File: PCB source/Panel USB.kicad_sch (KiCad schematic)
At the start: 9 parts, among them J4 Connector, USB-TYPE-C-16P, U12 IP4234CZ6

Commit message: Pass ERC
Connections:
- net FRONT_PANEL.D+ renamed FRONT_PANEL.+
- net FRONT_PANEL.D- renamed FRONT_PANEL.-
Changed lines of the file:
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@@
 		)
 	)
-	(label "FRONT_PANEL.D+"
+	(label "FRONT_PANEL.+"
 		(at 194.31 99.06 180)
 		(fields_autoplaced yes)
@@
 		)
 	)
-	(label "FRONT_PANEL.D-"
+	(label "FRONT_PANEL.-"
 		(at 194.31 101.6 180)
 		(fields_autoplaced yes)

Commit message: Prepare board for layout
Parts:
- removed J4: Connector, USB-TYPE-C-16P, USB_C_Upright16pin:MOLEX_2169890001, symbol PCM_JLCPCB-Extended:Connector, USB-TYPE-C-16P
- added J5: Connector, USB-TYPE-C-16P, PCM_JLCPCB:TYPE-C-SMD_HX-TYPE-C-16PIN, symbol PCM_JLCPCB-Extended:Connector, USB-TYPE-C-16P
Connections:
- net GND: now also J5.A12B1 (GND), J5.B12A1 (GND)
- net VBUS_IN: now also J5.A9B4 (VBUS), J5.B9A4 (VBUS)
- net at C55.1, R31.1: now also J5.S1 (SHIELD)
- net at R29.1: now also J5.A7 (D-), J5.B7 (D-)
- net at R28.1: now also J5.A5 (CC1)
- net at R30.1: now also J5.A6 (D+), J5.B6 (D+)
- net at R27.1: now also J5.B5 (CC2)
- net FRONT_PANEL.+ renamed FRONT_PANEL.D-
- net FRONT_PANEL.- renamed FRONT_PANEL.D+
- net USB_IN.+ renamed USB_IN.D+
- net USB_IN.- renamed USB_IN.D-
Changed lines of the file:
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@@
 		)
 	)
-	(label "FRONT_PANEL.+"
-		(at 194.31 99.06 180)
+	(label "FRONT_PANEL.D+"
+		(at 193.04 101.6 180)
+		(fields_autoplaced yes)
+		(effects
+			(font
+				(size 1.27 1.27)
+			)
+			(justify right bottom)
+		)
+	)
+	(label "FRONT_PANEL.D-"
+		(at 193.04 99.06 180)
 		(fields_autoplaced yes)
 		(effects
@@
 		)
 	)
-	(label "USB_IN.+"
+	(label "USB_IN.D+"
 		(at 140.97 88.9 180)
 		(fields_autoplaced yes)
@@
 		)
 	)
-	(label "FRONT_PANEL.-"
-		(at 194.31 101.6 180)
-		(fields_autoplaced yes)
-		(effects
-			(font
-				(size 1.27 1.27)
-			)
-			(justify right bottom)
-		)
-	)
-	(label "USB_IN.-"
+	(label "USB_IN.D-"
 		(at 140.97 83.82 180)
 		(fields_autoplaced yes)
@@
 	)
 	(symbol
-		(lib_id "PCM_JLCPCB-Extended:Connector, USB-TYPE-C-16P")
-		(at 96.52 85.09 0)
-		(unit 1)
-		(exclude_from_sim no)
-		(in_bom yes)
-		(on_board yes)
-		(dnp no)
-		(fields_autoplaced yes)
-		(property "Reference" "J4"
-			(at 96.52 64.77 0)
-			(effects
-				(font
-					(size 1.27 1.27)
-				)
-			)
-		)
-		(property "Value" "Connector, USB-TYPE-C-16P"
-			(at 99.06 86.36 0)
-			(effects
-				(font
-					(size 1.27 1.27)
-				)
-				(hide yes)
-			)
-		)
-		(property "Footprint" "USB_C_Upright16pin:MOLEX_2169890001"
-			(at 96.52 95.25 0)
-			(effects
-				(font
-					(size 1.27 1.27)
-					(italic yes)
-				)
-				(hide yes)
-			)
-		)
-		(property "Datasheet" "https://atta.szlcsc.com/upload/public/pdf/source/20220920/0EF8F885FCCEA71F60E9E85152155021.pdf"
-			(at 94.234 84.963 0)
-			(effects
-				(font
-					(size 1.27 1.27)
-				)
-				(justify left)
-				(hide yes)
-			)
-		)
-		(property "Description" "3A 1 Horizontal attachment 16P Female -25℃~+85℃ Type-C SMD USB Connectors ROHS"
-			(at 99.06 83.82 0)
-			(effects
-				(font
-					(size 1.27 1.27)
-				)
-				(hide yes)
-			)
-		)
-		(property "LCSC" "C2927039"
-			(at 99.06 83.82 0)
-			(effects
-				(font
-					(size 1.27 1.27)
-				)
-				(hide yes)
-			)
-		)
-		(pin "A8"
-		)
-		(pin "B6"
-		)
-		(pin "B5"
-		)
-		(pin "A5"
-		)
-		(pin "A7"
-		)
-		(pin "A6"
-		)
-		(pin "B7"
-		)
-		(pin "B8"
-		)
-		(pin "S1"
-		)
-		(pin "A12B1"
-		)
-		(pin "B9A4"
-		)
-		(pin "B12A1"
-		)
-		(pin "A9B4"
-		)
-		(instances
-			(project "OrangePie"
-				(path "/3103c9de-f1ba-4d51-8bfc-798df1c75e2f/86d81324-cbad-4692-8b67-2c038a3e8215"
-					(reference "J4")
-					(unit 1)
-				)
-			)
-		)
-	)
-	(symbol
 		(lib_id "power:GND")
 		(at 96.52 125.73 0)
@@
 					(unit 1)
 				)
+			)
+		)
+	)
+	(symbol
+		(lib_id "PCM_JLCPCB-Extended:Connector, USB-TYPE-C-16P")
+		(at 96.52 85.09 0)
+		(unit 1)
+		(exclude_from_sim no)
+		(in_bom yes)
+		(on_board yes)
+		(dnp no)
+		(fields_autoplaced yes)
+		(property "Reference" "J5"
+			(at 96.52 64.77 0)
+			(effects
+				(font
+					(size 1.27 1.27)
+				)
+			)
+		)
+		(property "Value" "Connector, USB-TYPE-C-16P"
+			(at 99.06 86.36 0)
+			(effects
+				(font
+					(size 1.27 1.27)
+				)
+				(hide yes)
+			)
+		)
+		(property "Footprint" "PCM_JLCPCB:TYPE-C-SMD_HX-TYPE-C-16PIN"
+			(at 96.52 95.25 0)
+			(effects
+				(font
+					(size 1.27 1.27)
+					(italic yes)
+				)
+				(hide yes)
+			)
+		)
+		(property "Datasheet" "https://atta.szlcsc.com/upload/public/pdf/source/20220920/0EF8F885FCCEA71F60E9E85152155021.pdf"
+			(at 94.234 84.963 0)
+			(effects
+				(font
+					(size 1.27 1.27)
+				)
+				(justify left)
+				(hide yes)
+			)
+		)
+		(property "Description" "3A 1 Horizontal attachment 16P Female -25℃~+85℃ Type-C SMD USB Connectors ROHS"
+			(at 99.06 83.82 0)
+			(effects
+				(font
+					(size 1.27 1.27)
+				)
+				(hide yes)
+			)
+		)
+		(property "LCSC" "C2927039"
+			(at 99.06 83.82 0)
+			(effects
+				(font
+					(size 1.27 1.27)
+				)
+				(hide yes)
+			)
+		)
+		(pin "A6"
+		)
+		(pin "A12B1"
+		)
+		(pin "S1"
+		)
+		(pin "B8"
+		)
+		(pin "B12A1"
+		)
+		(pin "A9B4"
+		)
+		(pin "A7"
+		)
+		(pin "A5"
+		)
+		(pin "A8"
+		)
+		(pin "B6"
+		)
+		(pin "B7"
+		)
+		(pin "B9A4"
+		)
+		(pin "B5"
+		)
+		(instances
+			(project ""
+				(path "/3103c9de-f1ba-4d51-8bfc-798df1c75e2f/86d81324-cbad-4692-8b67-2c038a3e8215"
+					(reference "J5")
+					(unit 1)
+				)

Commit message: Create v1 floorplan
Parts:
- J5: footprint PCM_JLCPCB:TYPE-C-SMD_HX-TYPE-C-16PIN -> Connector_USB:USB_C_Receptacle_GCT_USB4105-xx-A_16P_TopMnt_Horizontal
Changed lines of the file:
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@@
 			)
 		)
-		(property "Footprint" "PCM_JLCPCB:TYPE-C-SMD_HX-TYPE-C-16PIN"
+		(property "Footprint" "Connector_USB:USB_C_Receptacle_GCT_USB4105-xx-A_16P_TopMnt_Horizontal"
 			(at 96.52 95.25 0)
 			(effects

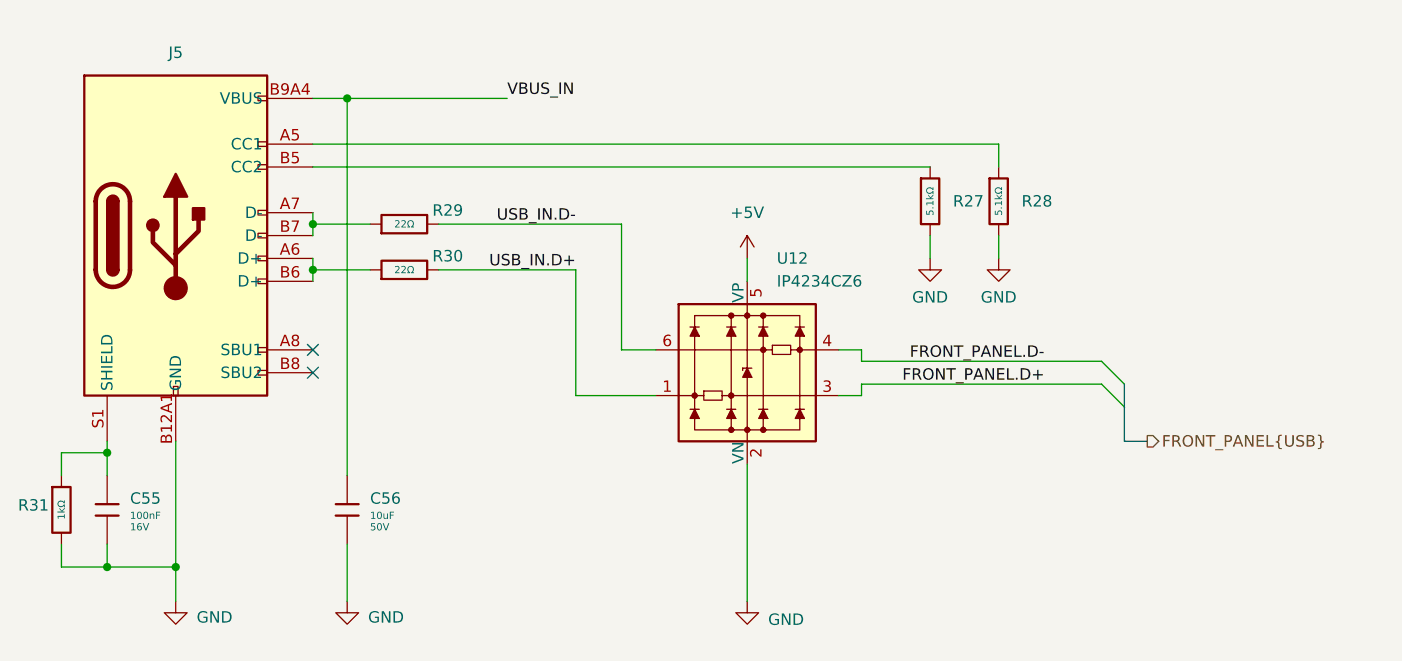
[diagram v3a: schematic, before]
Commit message: Do signal layer layout
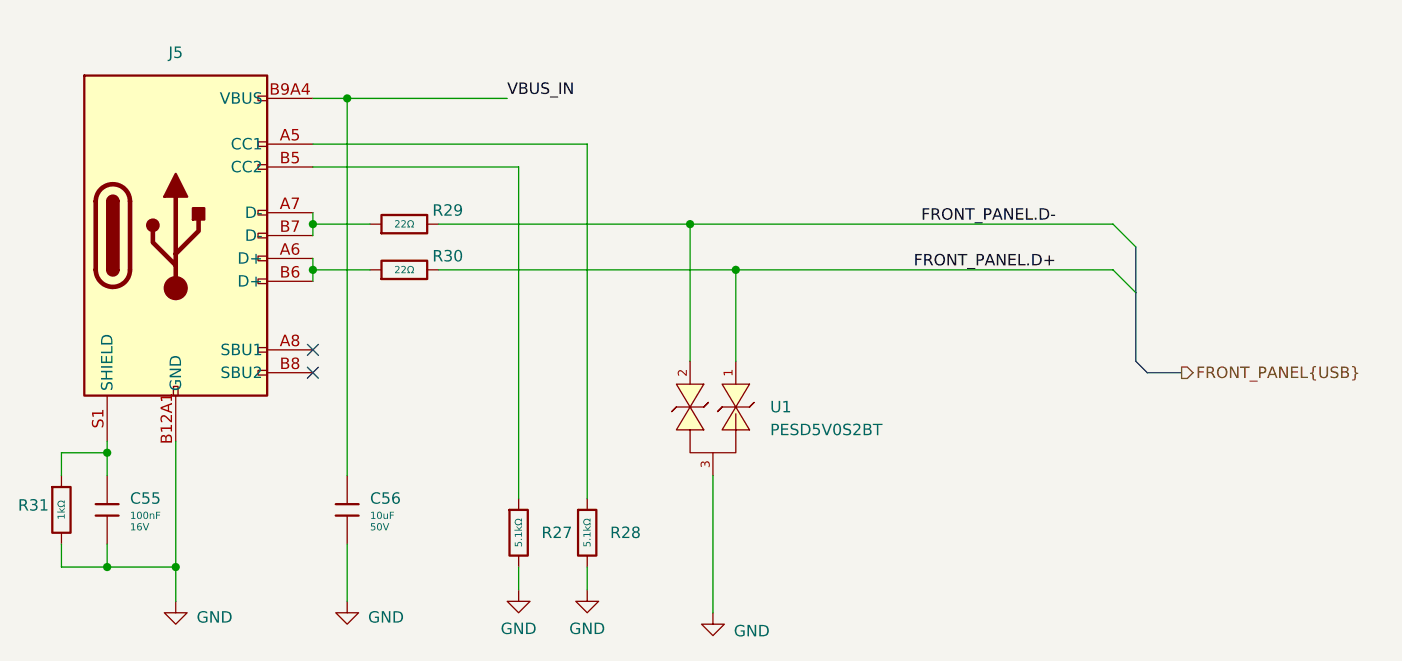
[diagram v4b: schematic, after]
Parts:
- removed U12: IP4234CZ6, Package_TO_SOT_SMD:SC-74-6_1.55x2.9mm_P0.95mm, symbol Power_Protection:IP4234CZ6
- added U1: PESD5V0S2BT, Package_TO_SOT_SMD:SOT-23, symbol PESD5V0S2BT:PESD5V0S2BT
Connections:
- net USB_IN.D+ is gone; now on net FRONT_PANEL.D+: R30.2
- net USB_IN.D- is gone; now on net FRONT_PANEL.D-: R29.2
- net FRONT_PANEL.D+: now also U1.1
- net FRONT_PANEL.D-: now also U1.2
- net GND: now also U1.3
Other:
- moved on the sheet: R27, R28

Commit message: Finish layout
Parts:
- removed J5: Connector, USB-TYPE-C-16P, Connector_USB:USB_C_Receptacle_GCT_USB4105-xx-A_16P_TopMnt_Horizontal, symbol PCM_JLCPCB-Extended:Connector, USB-TYPE-C-16P
- added J5: USB_C_Receptacle_USB2.0_16P, Connector_USB:USB_C_Receptacle_GCT_USB4105-xx-A_16P_TopMnt_Horizontal, symbol Connector:USB_C_Receptacle_USB2.0_16P
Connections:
- net GND: now also J5.A1 (GND), J5.A12 (GND), J5.B1 (GND), J5.B12 (GND)
- net VBUS_IN: now also J5.A4 (VBUS), J5.A9 (VBUS), J5.B4 (VBUS), J5.B9 (VBUS)
- net at C55.1, R31.1: now also J5.S1 (SHIELD)
- net at R29.1: now also J5.A7 (D-), J5.B7 (D-)
- net at R28.1: now also J5.A5 (CC1)
- net at R30.1: now also J5.A6 (D+), J5.B6 (D+)
- net at R27.1: now also J5.B5 (CC2)
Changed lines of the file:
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@@
-	)
-	(symbol
-		(lib_id "PCM_JLCPCB-Extended:Connector, USB-TYPE-C-16P")
-		(at 96.52 85.09 0)
-		(unit 1)
-		(exclude_from_sim no)
-		(in_bom yes)
-		(on_board yes)
-		(dnp no)
-		(fields_autoplaced yes)
-		(property "Reference" "J5"
-			(at 96.52 64.77 0)
-			(effects
-				(font
-					(size 1.27 1.27)
-				)
-			)
-		)
-		(property "Value" "Connector, USB-TYPE-C-16P"
-			(at 99.06 86.36 0)
-			(effects
-				(font
-					(size 1.27 1.27)
-				)
-				(hide yes)
-			)
-		)
-		(property "Footprint" "Connector_USB:USB_C_Receptacle_GCT_USB4105-xx-A_16P_TopMnt_Horizontal"
-			(at 96.52 95.25 0)
-			(effects
-				(font
-					(size 1.27 1.27)
-					(italic yes)
-				)
-				(hide yes)
-			)
-		)
-		(property "Datasheet" "https://atta.szlcsc.com/upload/public/pdf/source/20220920/0EF8F885FCCEA71F60E9E85152155021.pdf"
-			(at 94.234 84.963 0)
-			(effects
-				(font
-					(size 1.27 1.27)
-				)
-				(justify left)
-				(hide yes)
-			)
-		)
-		(property "Description" "3A 1 Horizontal attachment 16P Female -25℃~+85℃ Type-C SMD USB Connectors ROHS"
-			(at 99.06 83.82 0)
-			(effects
-				(font
-					(size 1.27 1.27)
-				)
-				(hide yes)
-			)
-		)
-		(property "LCSC" "C2927039"
-			(at 99.06 83.82 0)
-			(effects
-				(font
-					(size 1.27 1.27)
-				)
-				(hide yes)
-			)
-		)
-		(pin "A6"
-		)
-		(pin "A12B1"
-		)
-		(pin "S1"
-		)
-		(pin "B8"
-		)
-		(pin "B12A1"
-		)
-		(pin "A9B4"
-		)
-		(pin "A7"
-		)
-		(pin "A5"
-		)
-		(pin "A8"
-		)
-		(pin "B6"
-		)
-		(pin "B7"
-		)
-		(pin "B9A4"
-		)
-		(pin "B5"
-		)
-		(instances
-			(project ""
-				(path "/3103c9de-f1ba-4d51-8bfc-798df1c75e2f/86d81324-cbad-4692-8b67-2c038a3e8215"
-					(reference "J5")
-					(unit 1)
-				)
-			)
-		)
 	)
 	(symbol
@@
 					(unit 1)
 				)
+			)
+		)
+	)
+	(symbol
+		(lib_name "USB_C_Receptacle_USB2.0_16P_1")
+		(lib_id "Connector:USB_C_Receptacle_USB2.0_16P")
+		(at 96.52 85.09 0)
+		(unit 1)
+		(exclude_from_sim no)
+		(in_bom yes)
+		(on_board yes)
+		(dnp no)
+		(fields_autoplaced yes)
+		(property "Reference" "J5"
+			(at 96.52 62.23 0)
+			(effects
+				(font
+					(size 1.27 1.27)
+				)
+			)
+		)
+		(property "Value" "USB_C_Receptacle_USB2.0_16P"
+			(at 96.52 64.77 0)
+			(effects
+				(font
+					(size 1.27 1.27)
+				)
+			)
+		)
+		(property "Footprint" "Connector_USB:USB_C_Receptacle_GCT_USB4105-xx-A_16P_TopMnt_Horizontal"
+			(at 100.33 85.09 0)
+			(effects
+				(font
+					(size 1.27 1.27)
+				)
+				(hide yes)
+			)
+		)
+		(property "Datasheet" "https://www.usb.org/sites/default/files/documents/usb_type-c.zip"
+			(at 100.33 85.09 0)
+			(effects
+				(font
+					(size 1.27 1.27)
+				)
+				(hide yes)
+			)
+		)
+		(property "Description" "USB 2.0-only 16P Type-C Receptacle connector"
+			(at 96.52 85.09 0)
+			(effects
+				(font
+					(size 1.27 1.27)
+				)
+				(hide yes)
+			)
+		)
+		(pin "A4"
+		)
+		(pin "B9"
+		)
+		(pin "A8"
+		)
+		(pin "A9"
+		)
+		(pin "B1"
+		)
+		(pin "S1"
+		)
+		(pin "A1"
+		)
+		(pin "B12"
+		)
+		(pin "A7"
+		)
+		(pin "B6"
+		)
+		(pin "B8"
+		)
+		(pin "A5"
+		)
+		(pin "A6"
+		)
+		(pin "B5"
+		)
+		(pin "B4"
+		)
+		(pin "B7"
+		)
+		(pin "A12"
+		)
+		(instances
+			(project "OrangePie"
+				(path "/3103c9de-f1ba-4d51-8bfc-798df1c75e2f/86d81324-cbad-4692-8b67-2c038a3e8215"
+					(reference "J5")
+					(unit 1)
+				)

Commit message: Fix schematic
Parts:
- removed U1: PESD5V0S2BT, Package_TO_SOT_SMD:SOT-23, symbol PESD5V0S2BT:PESD5V0S2BT
- added U402: TPD2E2U06DCK, Package_TO_SOT_SMD:SOT-323_SC-70, symbol Power_Protection:TPD2E2U06DCK
- C55: Stock 27771805 -> 19831671
- C56: Price 0.067USD -> 0.069USD; Stock 1423931 -> 1211974
- R27, R28: Stock 2578203 -> 3416329
- R29, R30: Stock 2497993 -> 2158519
- R31: Stock 10672962 -> 7947916
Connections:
- net FRONT_PANEL.D+: now also U402.1
- net FRONT_PANEL.D-: now also U402.2
- net GND: now also U402.3
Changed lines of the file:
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@@
 (kicad_sch
-	(version 20231120)
+	(version 20250114)
 	(generator "eeschema")
-	(generator_version "8.0")
+	(generator_version "9.0")
 	(paper "A4")
 	(title_block
@@
 		)
 	)
-	(wire
-		(pts
-			(xy 158.75 88.9) (xy 158.75 99.06)
-		)
-		(stroke
-			(width 0)
-			(type default)
-		)
-	)
-	(wire
-		(pts
-			(xy 153.67 83.82) (xy 153.67 99.06)
-		)
-		(stroke
-			(width 0)
-			(type default)
-		)
-	)
 	(bus
 		(pts
@@
 	(wire
 		(pts
+			(xy 153.67 105.41) (xy 161.29 105.41)
+		)
+		(stroke
+			(width 0)
+			(type default)
+		)
+	)
+	(wire
+		(pts
+			(xy 158.75 88.9) (xy 158.75 100.33)
+		)
+		(stroke
+			(width 0)
+			(type default)
+		)
+	)
+	(wire
+		(pts
 			(xy 111.76 88.9) (xy 111.76 90.17)
 		)
@@
 	(wire
 		(pts
-			(xy 156.21 111.76) (xy 156.21 127)
+			(xy 168.91 110.49) (xy 168.91 125.73)
 		)
 		(stroke
@@
 		(pts
 			(xy 111.76 83.82) (xy 111.76 85.09)
+		)
+		(stroke
+			(width 0)
+			(type default)
+		)
+	)
+	(wire
+		(pts
+			(xy 153.67 83.82) (xy 153.67 105.41)
+		)
+		(stroke
+			(width 0)
+			(type default)
+		)
+	)
+	(wire
+		(pts
+			(xy 158.75 100.33) (xy 161.29 100.33)
 		)
 		(stroke
@@
 	(label "FRONT_PANEL.D+"
 		(at 194.31 88.9 180)
-		(fields_autoplaced yes)
 		(effects
 			(font
@@
 	(label "FRONT_PANEL.D-"
 		(at 194.31 83.82 180)
-		(fields_autoplaced yes)
 		(effects
 			(font
@@
 	(label "VBUS_IN"
 		(at 133.35 69.85 0)
-		(fields_autoplaced yes)
 		(effects
 			(font
@@
 		(shape output)
 		(at 208.28 100.33 0)
-		(fields_autoplaced yes)
 		(effects
 			(font
@@
 			)
 		)
-		(property "Stock" "27771805"
+		(property "Stock" "19831671"
 			(at 88.9 115.57 0)
 			(effects
@@
 			)
 		)
-		(property "Stock" "2497993"
+		(property "Stock" "2158519"
 			(at 121.92 83.82 0)
 			(effects
@@
 			)
 		)
-		(property "Stock" "2578203"
+		(property "Stock" "3416329"
 			(at 142.24 118.11 0)
 			(effects
@@
 	(symbol
 		(lib_id "power:GND")
-		(at 156.21 127 0)
+		(at 168.91 125.73 0)
 		(unit 1)
 		(exclude_from_sim no)
@@
 		(dnp no)
 		(property "Reference" "#PWR0117"
-			(at 156.21 133.35 0)
+			(at 168.91 132.08 0)
 			(effects
 				(font
@@
 		)
 		(property "Value" "GND"
-			(at 160.528 129.032 0)
+			(at 173.228 127.762 0)
 			(effects
 				(font
@@
 		)
 		(property "Footprint" ""
-			(at 156.21 127 0)
+			(at 168.91 125.73 0)
 			(effects
 				(font
@@
 		)
 		(property "Datasheet" ""
-			(at 156.21 127 0)
+			(at 168.91 125.73 0)
 			(effects
 				(font
@@
 		)
 		(property "Description" "Power symbol creates a global label with name \"GND\" , ground"
-			(at 156.21 127 0)
+			(at 168.91 125.73 0)
 			(effects
 				(font
@@
 			)
 		)
-		(property "Stock" "10672962"
+		(property "Stock" "7947916"
 			(at 83.82 115.57 0)
 			(effects
@@
 				(path "/3103c9de-f1ba-4d51-8bfc-798df1c75e2f/86d81324-cbad-4692-8b67-2c038a3e8215"
 					(reference "R31")
-					(unit 1)
-				)
-			)
-		)
-	)
-	(symbol
-		(lib_id "PESD5V0S2BT:PESD5V0S2BT")
-		(at 156.21 106.68 180)
-		(unit 1)
-		(exclude_from_sim no)
-		(in_bom yes)
-		(on_board yes)
-		(dnp no)
-		(fields_autoplaced yes)
-		(property "Reference" "U1"
-			(at 162.56 104.1399 0)
-			(effects
-				(font
-					(size 1.27 1.27)
-				)
-				(justify right)
-			)
-		)
-		(property "Value" "PESD5V0S2BT"
-			(at 162.56 106.6799 0)
-			(effects
-				(font
-					(size 1.27 1.27)
-				)
-				(justify right)
-			)
-		)
-		(property "Footprint" "Package_TO_SOT_SMD:SOT-23"
-			(at 156.21 106.68 0)
-			(effects
-				(font
-					(size 1.27 1.27)
-				)
-				(hide yes)
-			)
-		)
-		(property "Datasheet" "https://www.lcsc.com/datasheet/lcsc_datasheet_2501101716_HXY-MOSFET-PESD5V0S2BT_C5451656.pdf"
-			(at 156.21 106.68 0)
-			(effects
-				(font
-					(size 1.27 1.27)
-				)
-				(hide yes)
-			)
-		)
-		(property "Description" "11A 8V 8V Bidirectional 5V SOT-23 ESD and Surge Protection (TVS/ESD)"
-			(at 156.21 106.68 0)
-			(effects
-				(font
-					(size 1.27 1.27)
-				)
-				(hide yes)
-			)
-		)
-		(pin "3"
-		)
-		(pin "1"
-		)
-		(pin "2"
-		)
-		(instances
-			(project "OrangePie"
-				(path "/3103c9de-f1ba-4d51-8bfc-798df1c75e2f/86d81324-cbad-4692-8b67-2c038a3e8215"
-					(reference "U1")
 					(unit 1)
 				)
@@
 			)
 		)
-		(property "Stock" "2497993"
+		(property "Stock" "2158519"
 			(at 121.92 88.9 0)
 			(effects
@@
 			)
 		)
-		(property "Stock" "1423931"
+		(property "Stock" "1211974"
 			(at 115.57 115.57 0)
 			(effects
@@
 			)
 		)
-		(property "Price" "0.067USD"
+		(property "Price" "0.069USD"
 			(at 115.57 115.57 0)
 			(effects
@@
 	)
 	(symbol
-		(lib_name "USB_C_Receptacle_USB2.0_16P_1")
+		(lib_id "Power_Protection:TPD2E2U06DCK")
+		(at 168.91 102.87 0)
+		(unit 1)
+		(exclude_from_sim no)
+		(in_bom yes)
+		(on_board yes)
+		(dnp no)
+		(fields_autoplaced yes)
+		(property "Reference" "U402"
+			(at 172.72 101.5999 0)
+			(effects
+				(font
+					(size 1.27 1.27)
+				)
+				(justify left)
+			)
+		)
+		(property "Value" "TPD2E2U06DCK"
+			(at 172.72 104.1399 0)
+			(effects
+				(font
+					(size 1.27 1.27)
+				)
+				(justify left)
+			)
+		)
+		(property "Footprint" "Package_TO_SOT_SMD:SOT-323_SC-70"
+			(at 148.59 109.22 0)
+			(effects
+				(font
+					(size 1.27 1.27)
+				)
+				(hide yes)
+			)
+		)
+		(property "Datasheet" "http://www.ti.com/lit/ds/symlink/tpd2e2u06.pdf"
+			(at 163.83 97.79 0)
+			(effects
+				(font
+					(size 1.27 1.27)
+				)
+				(hide yes)
+			)
+		)
+		(property "Description" "Dual-Channel High-Speed ESD Protection, SC-70"
+			(at 168.91 102.87 0)
+			(effects
+				(font
+					(size 1.27 1.27)
+				)
+				(hide yes)
+			)
+		)
+		(pin "2"
+		)
+		(pin "1"
+		)
+		(pin "3"
+		)
+		(instances
+			(project "OrangePie"
+				(path "/3103c9de-f1ba-4d51-8bfc-798df1c75e2f/86d81324-cbad-4692-8b67-2c038a3e8215"
+					(reference "U402")
+					(unit 1)
+				)
+			)
+		)
+	)
+	(symbol
 		(lib_id "Connector:USB_C_Receptacle_USB2.0_16P")
 		(at 96.52 85.09 0)
@@
 			)
 		)
-		(property "Stock" "2578203"
+		(property "Stock" "3416329"
 			(at 134.62 118.11 0)
 			(effects
